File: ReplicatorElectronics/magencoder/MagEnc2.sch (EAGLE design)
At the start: 9 parts, among them J1 SBH11-PBPC-D07-ST-BK, J2 70553-0037

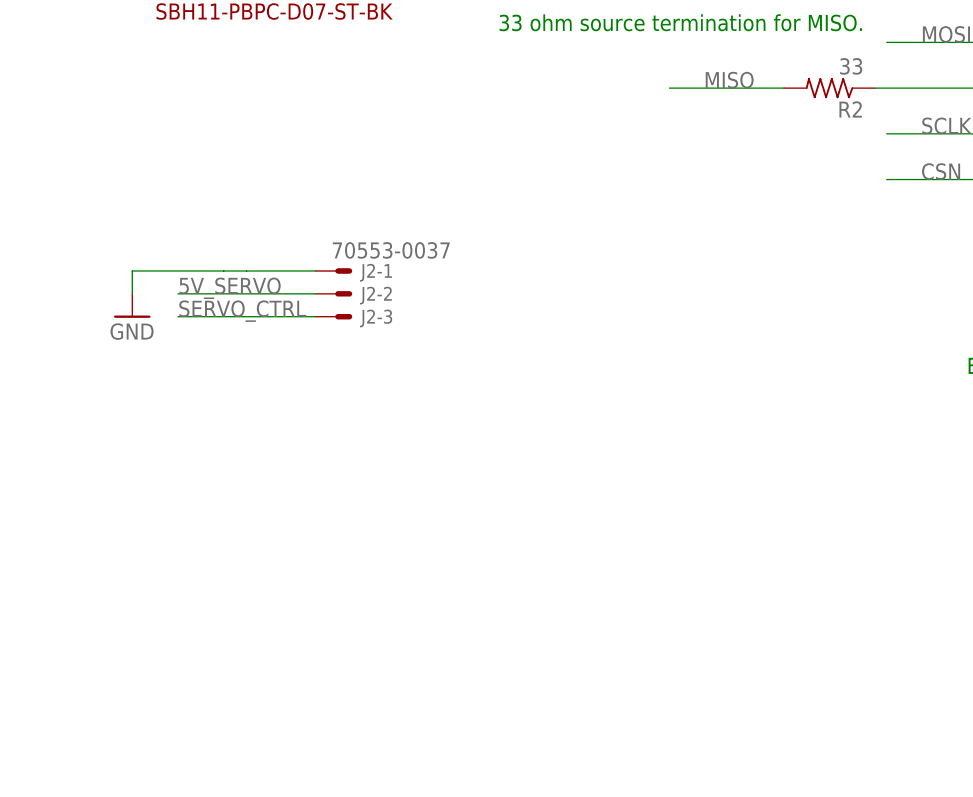
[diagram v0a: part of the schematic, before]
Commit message: 6/3/12: Added LED on CSN.
~ 0.5 hr.
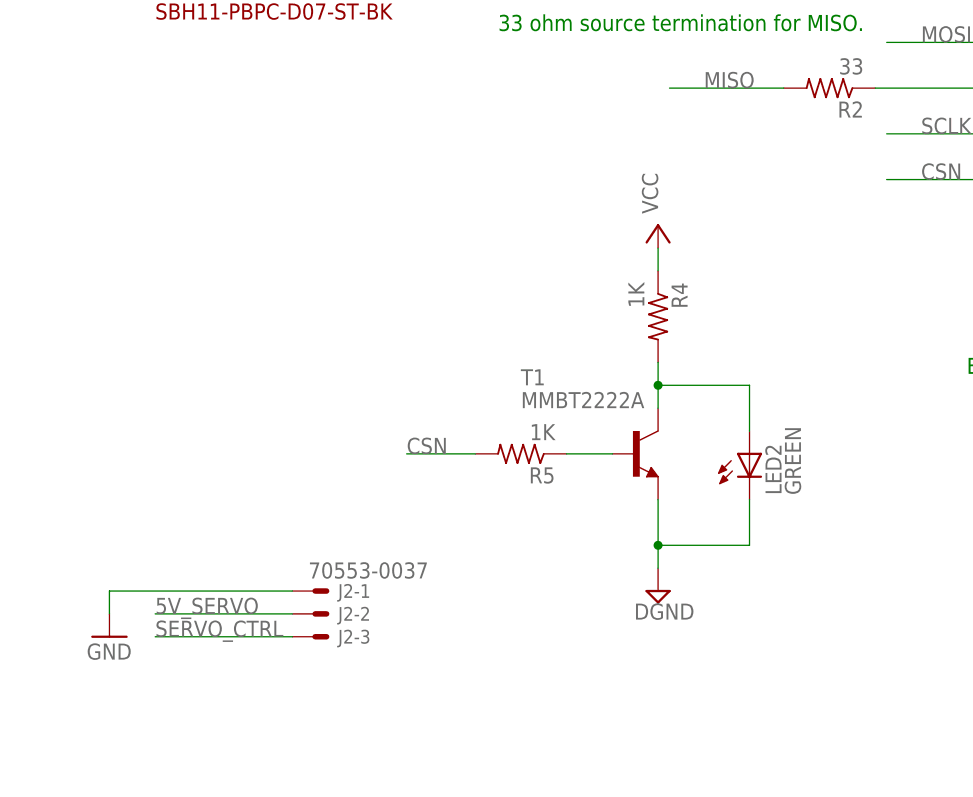
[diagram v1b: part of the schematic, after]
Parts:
- added LED2: GREEN, led:LEDCHIPLED_0805
- added R4, R5: 1K, rcl:R-US_R0603
- added T1: MMBT2222A, transistor:MMBT2222ALT1-NPN-SOT23-BEC
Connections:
- new net N$2: LED2.A, R4.2, T1.C
- new net N$3: R5.1, T1.B
- net CSN: now also R5.2
- net DGND: now also LED2.C, T1.E
- net VCC: now also R4.1
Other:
- moved on the sheet: J2-1, J2-2, J2-3
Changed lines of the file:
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@@
 <part name="GND1" library="supply1" deviceset="GND" device=""/>
 <part name="J1" library="SBH11-PBPC-D07-ST-BK" deviceset="SBH11-PBPC-D07-ST-BK" device=""/>
+<part name="T1" library="transistor" deviceset="*-NPN-" device="SOT23-BEC" technology="MMBT2222ALT1" value="MMBT2222A"/>
+<part name="R4" library="rcl" deviceset="R-US_" device="R0603" value="1K"/>
+<part name="P+2" library="supply1" deviceset="VCC" device=""/>
+<part name="R5" library="rcl" deviceset="R-US_" device="R0603" value="1K"/>
+<part name="SUPPLY5" library="supply2" deviceset="DGND" device=""/>
+<part name="LED2" library="led" deviceset="LED" device="CHIPLED_0805" value="GREEN"/>
 </parts>
 <sheets>
@@
 <instance part="SUPPLY3" gate="G$1" x="71.12" y="10.16"/>
 <instance part="SUPPLY4" gate="G$1" x="121.92" y="30.48"/>
-<instance part="J2" gate="-1" x="-55.88" y="5.08"/>
-<instance part="J2" gate="-2" x="-55.88" y="2.54"/>
-<instance part="J2" gate="-3" x="-55.88" y="0"/>
-<instance part="GND1" gate="1" x="-78.74" y="0"/>
+<instance part="J2" gate="-1" x="-58.42" y="-30.48"/>
+<instance part="J2" gate="-2" x="-58.42" y="-33.02"/>
+<instance part="J2" gate="-3" x="-58.42" y="-35.56"/>
+<instance part="GND1" gate="1" x="-81.28" y="-35.56"/>
 <instance part="J1" gate="G$1" x="-68.58" y="53.34"/>
+<instance part="T1" gate="G$1" x="-22.86" y="-15.24" smashed="yes">
+<attribute name="NAME" x="-35.56" y="-7.62" size="1.778" layer="95"/>
+<attribute name="VALUE" x="-35.56" y="-10.16" size="1.778" layer="96"/>
+</instance>
+<instance part="R4" gate="G$1" x="-20.32" y="0" rot="R270"/>
+<instance part="P+2" gate="VCC" x="-20.32" y="10.16" smashed="yes">
+<attribute name="VALUE" x="-20.32" y="11.43" size="1.778" layer="96" rot="R90"/>
+</instance>
+<instance part="R5" gate="G$1" x="-35.56" y="-15.24" rot="R180"/>
+<instance part="SUPPLY5" gate="G$1" x="-20.32" y="-30.48"/>
+<instance part="LED2" gate="G$1" x="-10.16" y="-15.24"/>
 </instances>
 <busses>
@@
 <segment>
 <pinref part="GND1" gate="1" pin="GND"/>
-<wire x1="-78.74" y1="2.54" x2="-78.74" y2="5.08" width="0.1524" layer="91"/>
+<wire x1="-81.28" y1="-33.02" x2="-81.28" y2="-30.48" width="0.1524" layer="91"/>
 <pinref part="J2" gate="-1" pin="S"/>
-<wire x1="-58.42" y1="5.08" x2="-66.04" y2="5.08" width="0.1524" layer="91"/>
-<wire x1="-66.04" y1="5.08" x2="-68.58" y2="5.08" width="0.1524" layer="91"/>
-<wire x1="-78.74" y1="5.08" x2="-68.58" y2="5.08" width="0.1524" layer="91"/>
+<wire x1="-81.28" y1="-30.48" x2="-60.96" y2="-30.48" width="0.1524" layer="91"/>
 </segment>
 </net>
@@
 <wire x1="137.16" y1="66.04" x2="121.92" y2="66.04" width="0.1524" layer="91"/>
 </segment>
+<segment>
+<pinref part="P+2" gate="VCC" pin="VCC"/>
+<pinref part="R4" gate="G$1" pin="1"/>
+<wire x1="-20.32" y1="7.62" x2="-20.32" y2="5.08" width="0.1524" layer="91"/>
+</segment>
 </net>
 <net name="CSN" class="0">
@@
 <label x="-83.82" y="53.34" size="1.778" layer="95"/>
 <pinref part="J1" gate="G$1" pin="7"/>
+</segment>
+<segment>
+<pinref part="R5" gate="G$1" pin="2"/>
+<wire x1="-40.64" y1="-15.24" x2="-48.26" y2="-15.24" width="0.1524" layer="91"/>
+<label x="-48.26" y="-15.24" size="1.778" layer="95"/>
 </segment>
 </net>
@@
 <segment>
 <pinref part="J2" gate="-2" pin="S"/>
-<wire x1="-58.42" y1="2.54" x2="-73.66" y2="2.54" width="0.1524" layer="91"/>
-<label x="-73.66" y="2.54" size="1.778" layer="95"/>
+<wire x1="-60.96" y1="-33.02" x2="-76.2" y2="-33.02" width="0.1524" layer="91"/>
+<label x="-76.2" y="-33.02" size="1.778" layer="95"/>
 </segment>
 </net>
@@
 <segment>
 <pinref part="J2" gate="-3" pin="S"/>
-<wire x1="-58.42" y1="0" x2="-73.66" y2="0" width="0.1524" layer="91"/>
-<label x="-73.66" y="0" size="1.778" layer="95"/>
+<wire x1="-60.96" y1="-35.56" x2="-76.2" y2="-35.56" width="0.1524" layer="91"/>
+<label x="-76.2" y="-35.56" size="1.778" layer="95"/>
 </segment>
 </net>
@@
 <wire x1="121.92" y1="35.56" x2="121.92" y2="33.02" width="0.1524" layer="91"/>
 </segment>
-</net>
+<segment>
+<pinref part="T1" gate="G$1" pin="E"/>
+<wire x1="-20.32" y1="-20.32" x2="-20.32" y2="-25.4" width="0.1524" layer="91"/>
+<pinref part="SUPPLY5" gate="G$1" pin="DGND"/>
+<pinref part="LED2" gate="G$1" pin="C"/>
+<wire x1="-20.32" y1="-25.4" x2="-20.32" y2="-27.94" width="0.1524" layer="91"/>
+<wire x1="-10.16" y1="-20.32" x2="-10.16" y2="-25.4" width="0.1524" layer="91"/>
+<wire x1="-10.16" y1="-25.4" x2="-20.32" y2="-25.4" width="0.1524" layer="91"/>
+<junction x="-20.32" y="-25.4"/>
+</segment>
+</net>
+<net name="N$2" class="0">
+<segment>
+<pinref part="LED2" gate="G$1" pin="A"/>
+<wire x1="-10.16" y1="-12.7" x2="-10.16" y2="-7.62" width="0.1524" layer="91"/>
+<pinref part="T1" gate="G$1" pin="C"/>
+<wire x1="-20.32" y1="-10.16" x2="-20.32" y2="-7.62" width="0.1524" layer="91"/>
+<pinref part="R4" gate="G$1" pin="2"/>
+<wire x1="-20.32" y1="-7.62" x2="-20.32" y2="-5.08" width="0.1524" layer="91"/>
+<wire x1="-10.16" y1="-7.62" x2="-20.32" y2="-7.62" width="0.1524" layer="91"/>
+<junction x="-20.32" y="-7.62"/>
+</segment>
+</net>
+<net name="N$3" class="0">
+<segment>
+<pinref part="T1" gate="G$1" pin="B"/>
+<wire x1="-25.4" y1="-15.24" x2="-30.48" y2="-15.24" width="0.1524" layer="91"/>
+<pinref part="R5" gate="G$1" pin="1"/>
+</segment>
+</net>

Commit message: 6/4/12: New, smaller size.
~ 1.5 hrs.
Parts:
- C1, C2: device rcl:C-EUC0805K -> resistor:C-USC0402
- LED1, LED2: device led:LEDCHIPLED_0805 -> resistor:R-US_R0402
- R1, R2, R3, R4, R5: device rcl:R-US_R0603 -> resistor:R-US_R0402
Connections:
- net DGND: now also LED1.2, LED2.2; no longer LED1.C, LED2.C
- net N$1: now also LED1.1; no longer LED1.A
- net N$2: now also LED2.1; no longer LED2.A
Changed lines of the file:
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@@
 <part name="U$2" library="AS5055" deviceset="AS5055" device=""/>
 <part name="P+1" library="supply1" deviceset="VCC" device=""/>
-<part name="R2" library="rcl" deviceset="R-US_" device="R0603" value="33"/>
-<part name="R3" library="rcl" deviceset="R-US_" device="R0603" value="15"/>
-<part name="R1" library="rcl" deviceset="R-US_" device="R0603" value="680"/>
-<part name="C1" library="rcl" deviceset="C-EU" device="C0805K" value="4.7u"/>
-<part name="C2" library="rcl" deviceset="C-EU" device="C0805K" value="100n"/>
-<part name="LED1" library="led" deviceset="LED" device="CHIPLED_0805" value="GREEN"/>
+<part name="R2" library="resistor" deviceset="R-US_" device="R0402" value="33"/>
+<part name="R3" library="resistor" deviceset="R-US_" device="R0402" value="15"/>
+<part name="R1" library="resistor" deviceset="R-US_" device="R0402" value="680"/>
+<part name="C1" library="resistor" deviceset="C-US" device="C0402" value="4.7u"/>
+<part name="C2" library="resistor" deviceset="C-US" device="C0402" value="100n"/>
 <part name="GND4" library="supply1" deviceset="GND" device=""/>
 <part name="SUPPLY1" library="supply2" deviceset="DGND" device=""/>
@@
 <part name="J1" library="SBH11-PBPC-D07-ST-BK" deviceset="SBH11-PBPC-D07-ST-BK" device=""/>
 <part name="T1" library="transistor" deviceset="*-NPN-" device="SOT23-BEC" technology="MMBT2222ALT1" value="MMBT2222A"/>
-<part name="R4" library="rcl" deviceset="R-US_" device="R0603" value="1K"/>
+<part name="R4" library="resistor" deviceset="R-US_" device="R0402" value="1K"/>
 <part name="P+2" library="supply1" deviceset="VCC" device=""/>
-<part name="R5" library="rcl" deviceset="R-US_" device="R0603" value="1K"/>
+<part name="R5" library="resistor" deviceset="R-US_" device="R0402" value="1K"/>
 <part name="SUPPLY5" library="supply2" deviceset="DGND" device=""/>
-<part name="LED2" library="led" deviceset="LED" device="CHIPLED_0805" value="GREEN"/>
+<part name="LED2" library="resistor" deviceset="R-US_" device="R0402" value="GREEN"/>
+<part name="LED1" library="resistor" deviceset="R-US_" device="R0402" value="GREEN"/>
 </parts>
 <sheets>
@@
 <instance part="C1" gate="G$1" x="121.92" y="43.18"/>
 <instance part="C2" gate="G$1" x="137.16" y="43.18"/>
-<instance part="LED1" gate="G$1" x="104.14" y="45.72"/>
 <instance part="GND4" gate="1" x="-27.94" y="63.5"/>
 <instance part="SUPPLY1" gate="G$1" x="-27.94" y="45.72"/>
@@
 <instance part="R5" gate="G$1" x="-35.56" y="-15.24" rot="R180"/>
 <instance part="SUPPLY5" gate="G$1" x="-20.32" y="-30.48"/>
-<instance part="LED2" gate="G$1" x="-10.16" y="-15.24"/>
+<instance part="LED2" gate="G$1" x="-10.16" y="-17.78" rot="R270"/>
+<instance part="LED1" gate="G$1" x="104.14" y="43.18" rot="R270"/>
 </instances>
 <busses>
@@
 <pinref part="R1" gate="G$1" pin="2"/>
 <wire x1="104.14" y1="50.8" x2="104.14" y2="48.26" width="0.1524" layer="91"/>
-<pinref part="LED1" gate="G$1" pin="A"/>
+<pinref part="LED1" gate="G$1" pin="1"/>
 </segment>
 </net>
@@
 </segment>
 <segment>
-<wire x1="104.14" y1="40.64" x2="104.14" y2="35.56" width="0.1524" layer="91"/>
+<wire x1="104.14" y1="38.1" x2="104.14" y2="35.56" width="0.1524" layer="91"/>
 <wire x1="104.14" y1="35.56" x2="121.92" y2="35.56" width="0.1524" layer="91"/>
-<pinref part="LED1" gate="G$1" pin="C"/>
 <pinref part="C1" gate="G$1" pin="2"/>
 <wire x1="121.92" y1="35.56" x2="137.16" y2="35.56" width="0.1524" layer="91"/>
@@
 <pinref part="SUPPLY4" gate="G$1" pin="DGND"/>
 <wire x1="121.92" y1="35.56" x2="121.92" y2="33.02" width="0.1524" layer="91"/>
+<pinref part="LED1" gate="G$1" pin="2"/>
 </segment>
 <segment>
@@
 <wire x1="-20.32" y1="-20.32" x2="-20.32" y2="-25.4" width="0.1524" layer="91"/>
 <pinref part="SUPPLY5" gate="G$1" pin="DGND"/>
-<pinref part="LED2" gate="G$1" pin="C"/>
 <wire x1="-20.32" y1="-25.4" x2="-20.32" y2="-27.94" width="0.1524" layer="91"/>
-<wire x1="-10.16" y1="-20.32" x2="-10.16" y2="-25.4" width="0.1524" layer="91"/>
+<wire x1="-10.16" y1="-22.86" x2="-10.16" y2="-25.4" width="0.1524" layer="91"/>
 <wire x1="-10.16" y1="-25.4" x2="-20.32" y2="-25.4" width="0.1524" layer="91"/>
 <junction x="-20.32" y="-25.4"/>
+<pinref part="LED2" gate="G$1" pin="2"/>
 </segment>
 </net>
 <net name="N$2" class="0">
 <segment>
-<pinref part="LED2" gate="G$1" pin="A"/>
+<pinref part="T1" gate="G$1" pin="C"/>
 <wire x1="-10.16" y1="-12.7" x2="-10.16" y2="-7.62" width="0.1524" layer="91"/>
-<pinref part="T1" gate="G$1" pin="C"/>
 <wire x1="-20.32" y1="-10.16" x2="-20.32" y2="-7.62" width="0.1524" layer="91"/>
 <pinref part="R4" gate="G$1" pin="2"/>
@@
 <wire x1="-10.16" y1="-7.62" x2="-20.32" y2="-7.62" width="0.1524" layer="91"/>
 <junction x="-20.32" y="-7.62"/>
-</segment>
-</net>
+<pinref part="LED2" gate="G$1" pin="1"/>
+</segment>
+</net>
